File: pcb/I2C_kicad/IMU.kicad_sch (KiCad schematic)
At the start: 0 parts

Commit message: I worked on the color sensor and also the gpio expander. I added the pull ups for the SDA and SCL on the color sensor so no need to add any more. Just put do not populate for the other I2c devices
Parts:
- added U2: ICM-42605, LGA14_2P5X3X0P91_IVS, symbol ICM-42605:ICM-42605
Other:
- company: (none) -> RoboCup
- title: (none) -> IMU

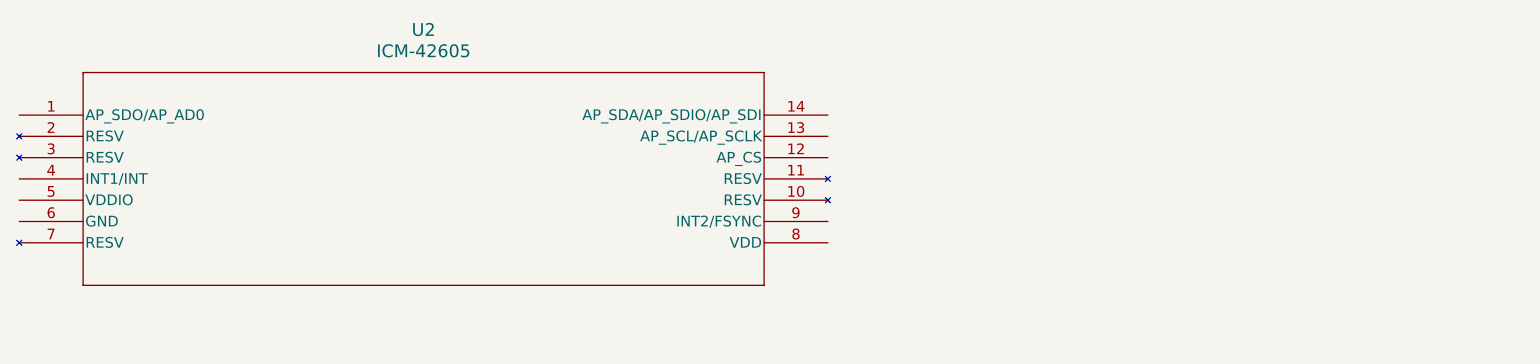
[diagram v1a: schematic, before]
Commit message: Add IMU, Hall effect, and temp sensor sheets
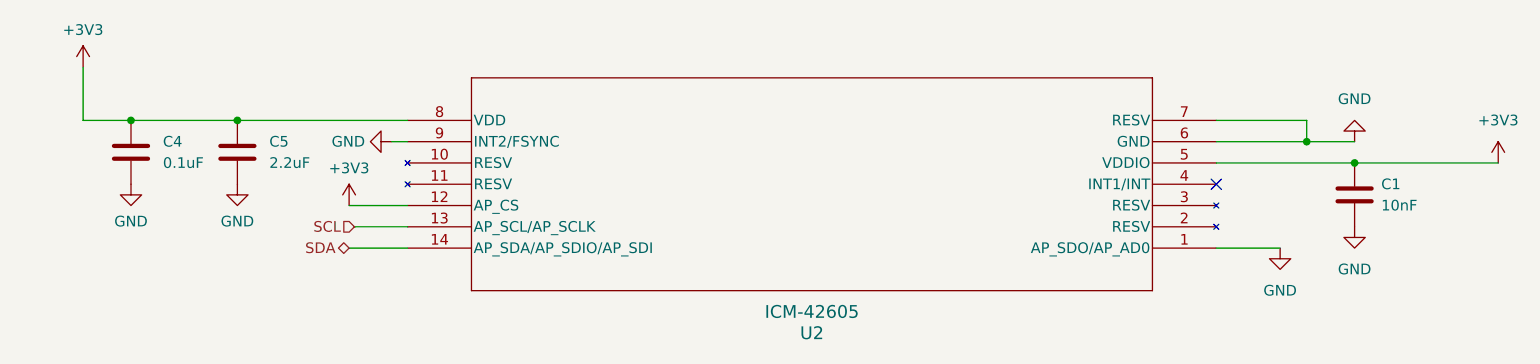
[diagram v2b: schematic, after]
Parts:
- added C1: 10nF, Capacitor_SMD:C_0603_1608Metric, symbol Device:C
- added C4: 0.1uF, Capacitor_SMD:C_0603_1608Metric, symbol Device:C
- added C5: 2.2uF, Capacitor_SMD:C_0603_1608Metric, symbol Device:C
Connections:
- net GND: now reaches U2.1 (AP_SDO/AP_AD0)
- net GND: now also U2.6 (GND), U2.7 (RESV), U2.9 (INT2/FSYNC), C1.2, C4.2, C5.2
- net +3V3: now reaches U2.12 (AP_CS)
- net +3V3: now also U2.5 (VDDIO), U2.8 (VDD), C1.1, C4.1, C5.1
- net SCL: now reaches U2.13 (AP_SCL/AP_SCLK)
- net SDA: now reaches U2.14 (AP_SDA/AP_SDIO/AP_SDI)
- no-connect marks 0 -> 1
